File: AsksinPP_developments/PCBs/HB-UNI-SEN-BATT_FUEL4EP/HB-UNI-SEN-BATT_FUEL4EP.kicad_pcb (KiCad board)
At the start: 2 copper layers, 75 x 75 mm, 29 parts, among them J1 Conn_01x02, J10 charge, J2 Conn_01x02, J3 Conn_01x02, J4 Conn_01x02, J5 ISP Programmer, J6 Conn_01x04, J7 Conn_01x04, J8 Conn_01x04, J9 Conn_01x04, Q1 IRLU024N, SW1 config button

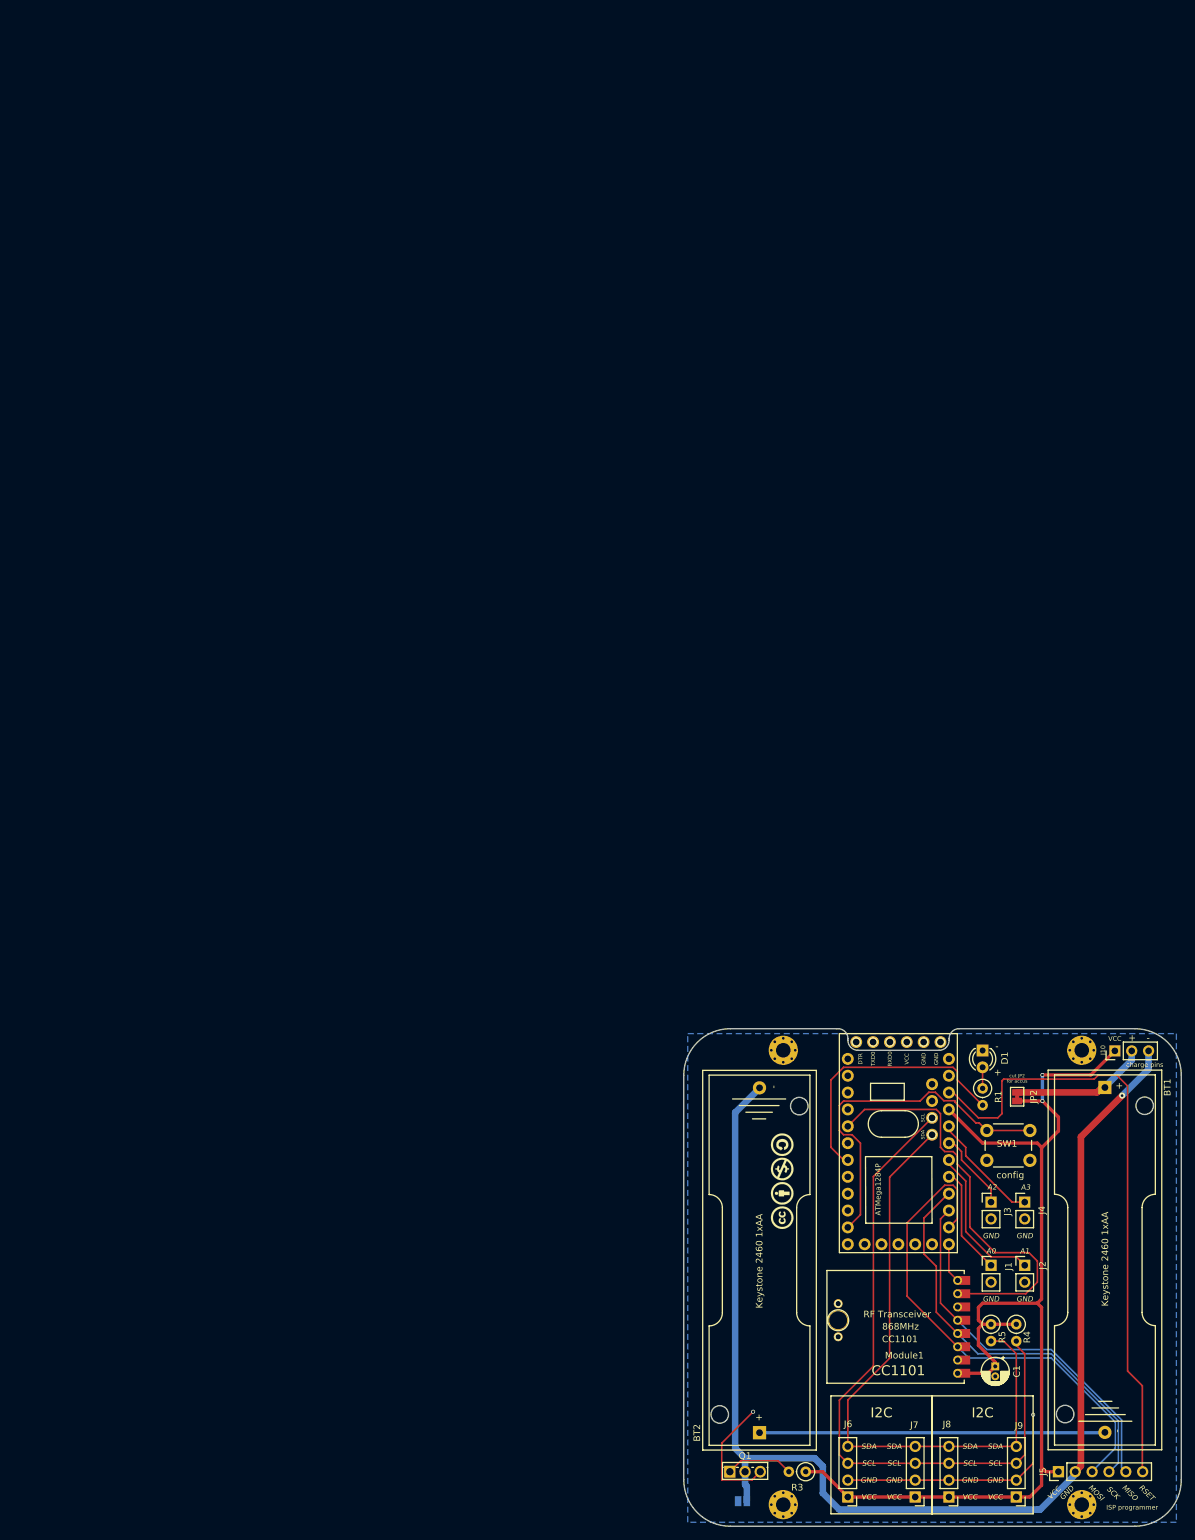
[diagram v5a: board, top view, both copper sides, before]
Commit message: PCBs: Fixes to ensure a proper production at JLCPCB, e.g. corrections of origins, rotations of assembled ICs etc.
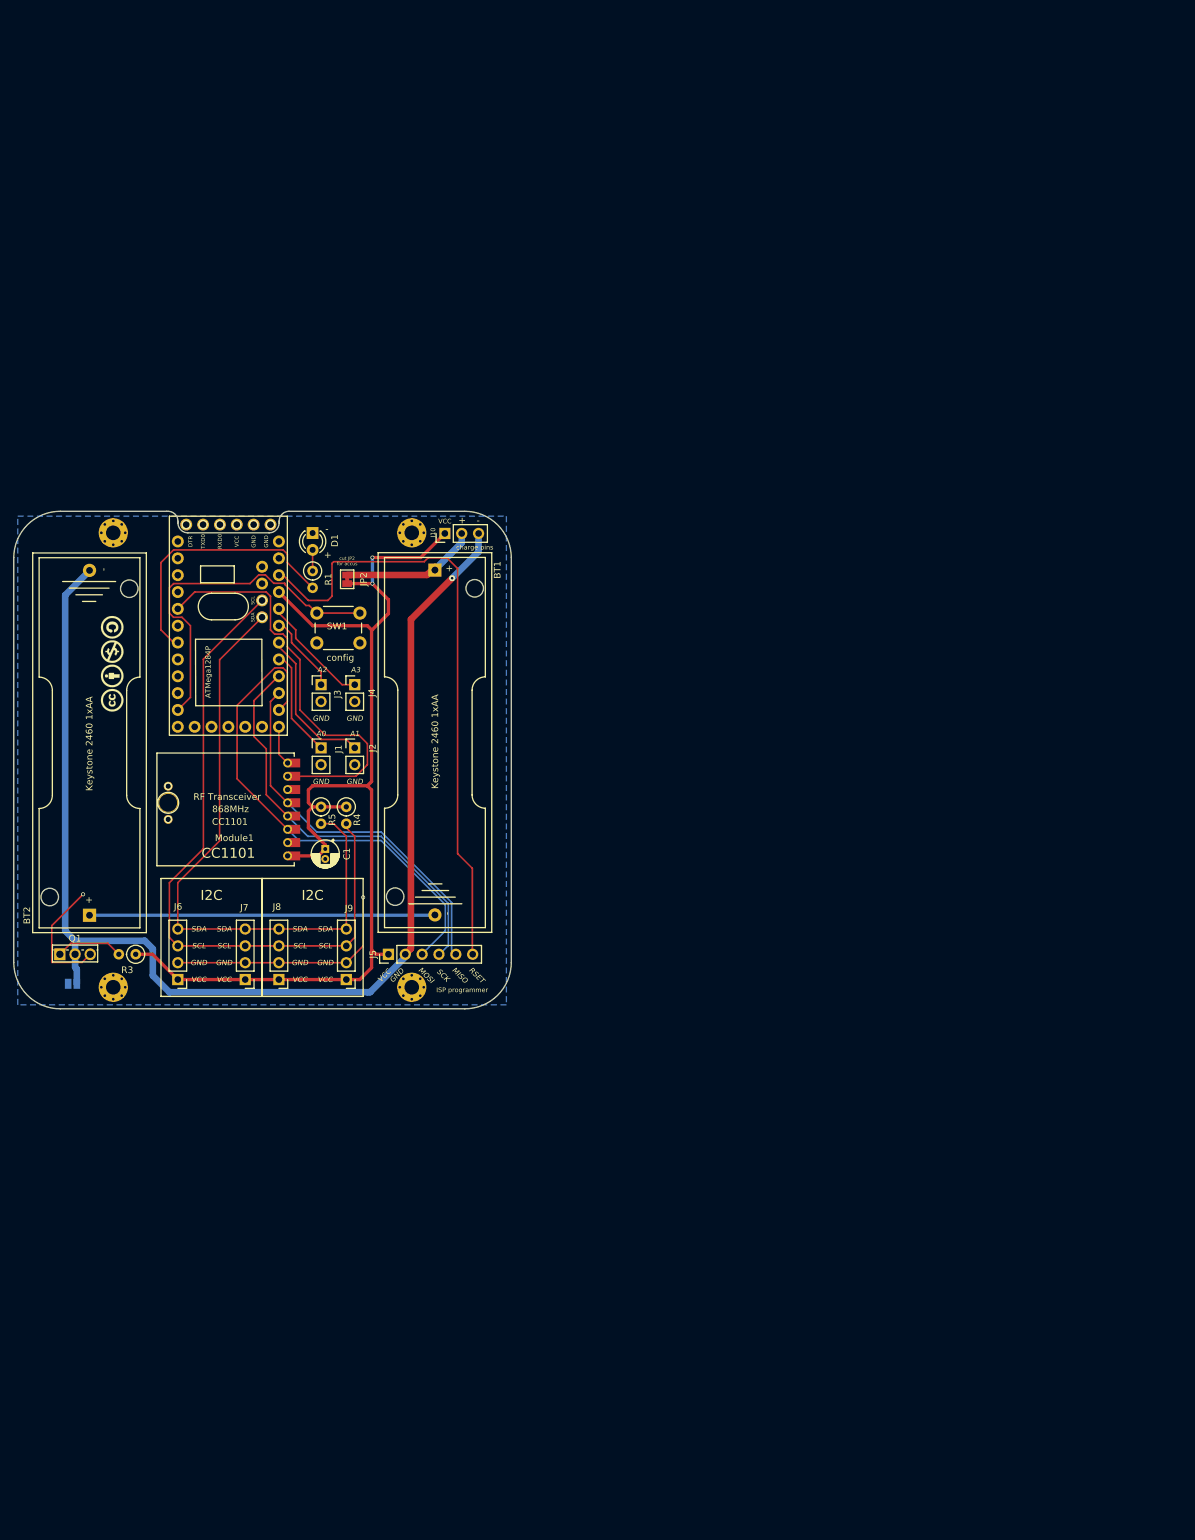
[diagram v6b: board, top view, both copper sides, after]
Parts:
- moved C1 127.6 mm to (47.0, 50.9)
- moved D1 127.6 mm to (45.0, 3.28)
- moved R1 127.6 mm to (45.0, 8.99)
- moved BT1 127.6 mm to (63.5, 8.86)
- moved BT2 127.6 mm to (11.4, 60.9)
- moved H1 127.6 mm to (15.0, 3.25)
- moved H2 127.6 mm to (60.0, 3.25)
- moved H3 127.6 mm to (15.0, 71.8)
- moved H4 127.6 mm to (60.0, 71.8)
- moved J1 127.6 mm to (46.3, 35.7)
- moved J10 127.6 mm to (65.0, 3.34)
- moved J2 127.6 mm to (51.4, 35.7)
- moved J3 127.6 mm to (46.3, 26.1)
- moved J4 127.6 mm to (51.4, 26.1)
- moved J5 127.6 mm to (56.5, 66.8)
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
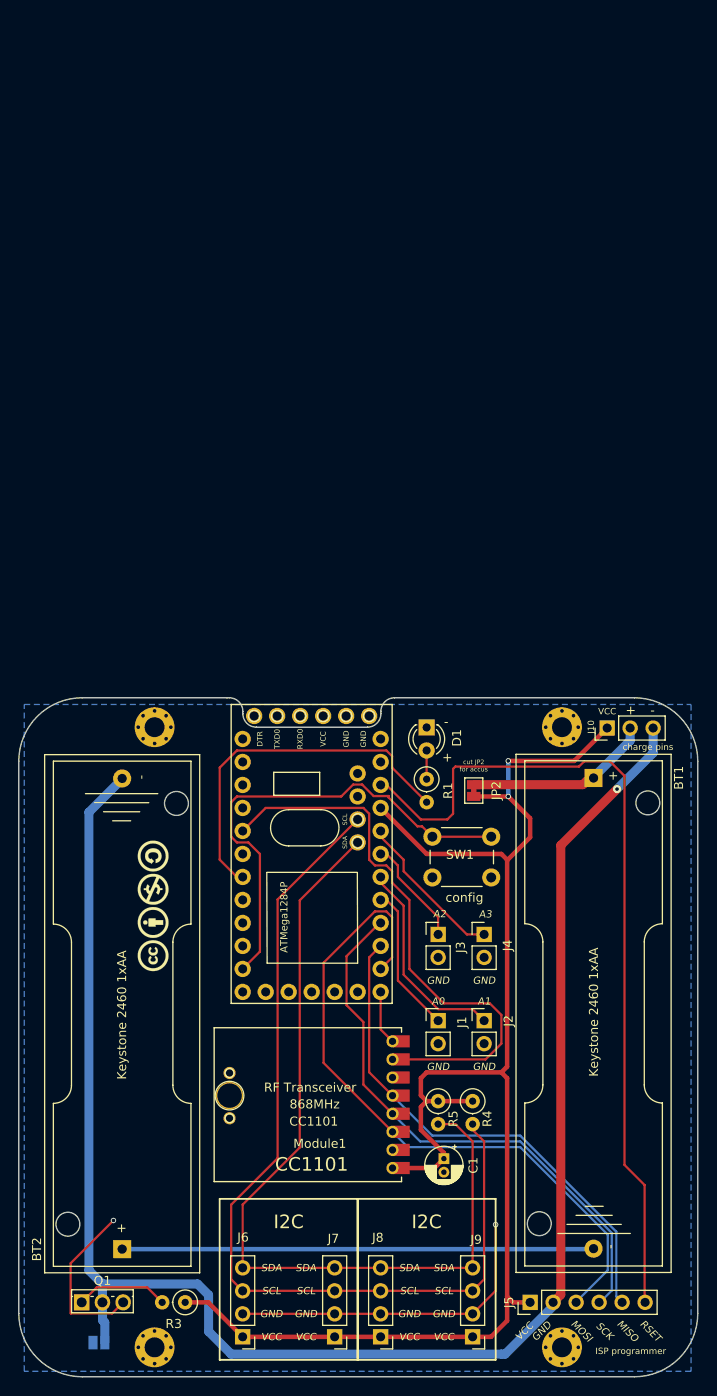
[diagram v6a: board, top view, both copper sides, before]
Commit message: PCBs: moved origin to lower left corner in order to fit to JLCPCB's scheme
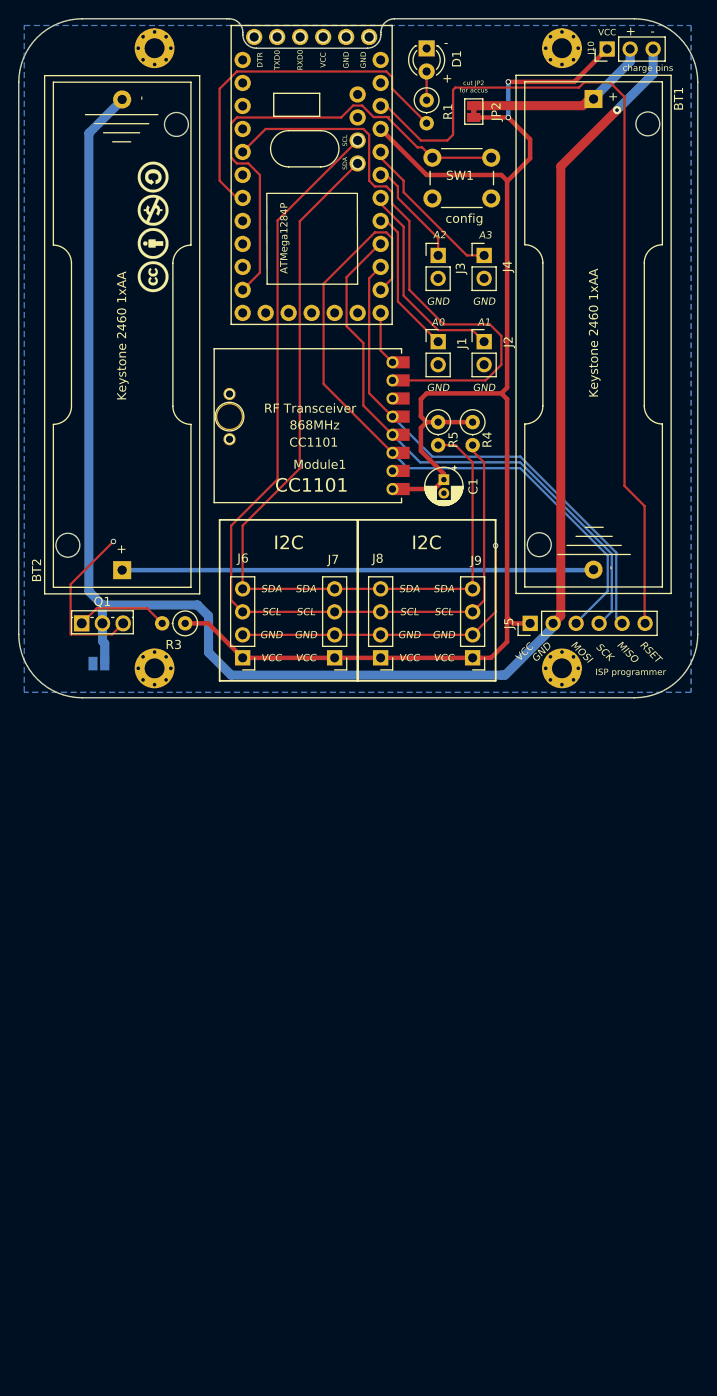
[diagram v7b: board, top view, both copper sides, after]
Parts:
- moved BT1 75.0 mm to (63.5, -66.1)
- moved BT2 75.0 mm to (11.4, -14.1)
- moved C1 75.0 mm to (47.0, -24.1)
- moved D1 75.0 mm to (45.0, -71.7)
- moved H1 75.0 mm to (15.0, -71.8)
- moved H2 75.0 mm to (60.0, -71.8)
- moved H3 75.0 mm to (15.0, -3.25)
- moved H4 75.0 mm to (60.0, -3.25)
- moved J1 75.0 mm to (46.3, -39.3)
- moved J10 75.0 mm to (65.0, -71.7)
- moved J2 75.0 mm to (51.4, -39.3)
- moved J3 75.0 mm to (46.3, -48.9)
- moved J4 75.0 mm to (51.4, -48.9)
- moved J5 75.0 mm to (56.5, -8.22)
- moved J6 75.0 mm to (24.7, -4.41)
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
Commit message: PCBs/HB-UNI-SEN-BATT_FUEL4EP: migration to KiCAD 8
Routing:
- net unconnected-(Module1-GD2-Pad6C): track 1.00 -> 0.00 mm
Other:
- board text added: "Version 1.3 - 09/2024 (KiCAD 8)"
- board text removed: "Version 1.2 - 07/2023 (KiCAD 6)"
